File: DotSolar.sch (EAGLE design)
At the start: 24 parts, among them IC1 CAT24M010TS, IC2 SI1145, Q1 BSH203, U1 ISL29125

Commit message: Update tracks for production at Aisler
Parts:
- D1: value (none) -> B130-13-F
- D3: value (none) -> 3.3V
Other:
- note added: "10-50mV Drop"
- note added: "200mV Drop"
- note removed: "100mV Drop"
- note removed: "50mV Drop"
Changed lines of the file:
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@@
 <part name="R2" library="rcl" deviceset="R-EU_" device="R0603" value="4.7kΩ"/>
 <part name="R3" library="rcl" deviceset="R-EU_" device="R0603" value="4.7kΩ"/>
-<part name="D3" library="diode" deviceset="ZENER-DIODE" device="SMB"/>
+<part name="D3" library="diode" deviceset="ZENER-DIODE" device="SMB" value="3.3V"/>
 <part name="Q1" library="BSH203" deviceset="BSH203" device=""/>
 <part name="U1" library="SparkFun-Sensors" deviceset="ISL29125" device=""/>
@@
 <part name="U$5" library="redan" deviceset="INA226" device=""/>
 <part name="R4" library="rcl" deviceset="R-EU_" device="R0603" value="4.7kΩ"/>
-<part name="D1" library="PP_Passives" deviceset="DIODE" device="_B130-13-F"/>
+<part name="D1" library="PP_Passives" deviceset="DIODE" device="_B130-13-F" value="B130-13-F"/>
 <part name="JP2" library="SparkFun-Jumpers" deviceset="JUMPER-SMT_2_NO" device="_SILK" value="NoBattery, only Capacitor"/>
 <part name="U$6" library="IXYS_Solar_cells" deviceset="KXOB22-01X8F_EXTENDED_PADS" device=""/>
@@
 <sheet>
 <plain>
-<text x="86.36" y="66.04" size="1.016" layer="91">50mV Drop</text>
-<text x="93.98" y="60.96" size="1.016" layer="91">100mV Drop</text>
+<text x="86.36" y="66.04" size="0.6096" layer="91">10-50mV Drop</text>
+<text x="93.98" y="60.96" size="0.6096" layer="91">200mV Drop</text>
 <text x="175.26" y="78.74" size="1.778" layer="91">Pullups</text>
 <text x="149.86" y="111.76" size="1.778" layer="91">Address 0x52 and 0x53(upper)</text>

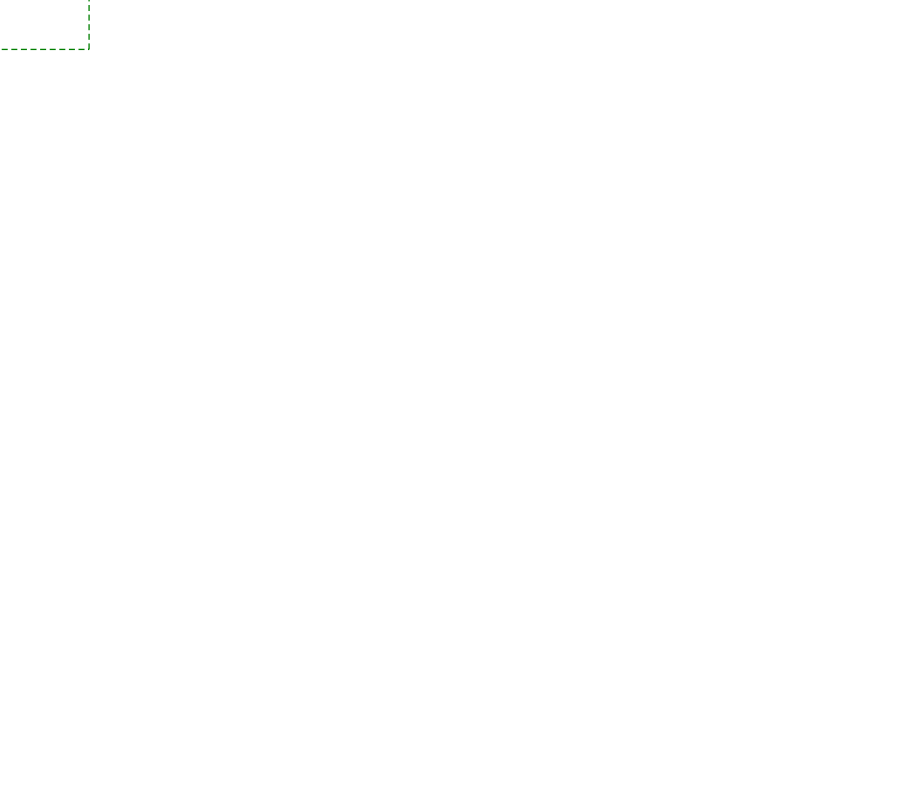
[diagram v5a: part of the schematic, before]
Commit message: Add AS3935 lightning detector
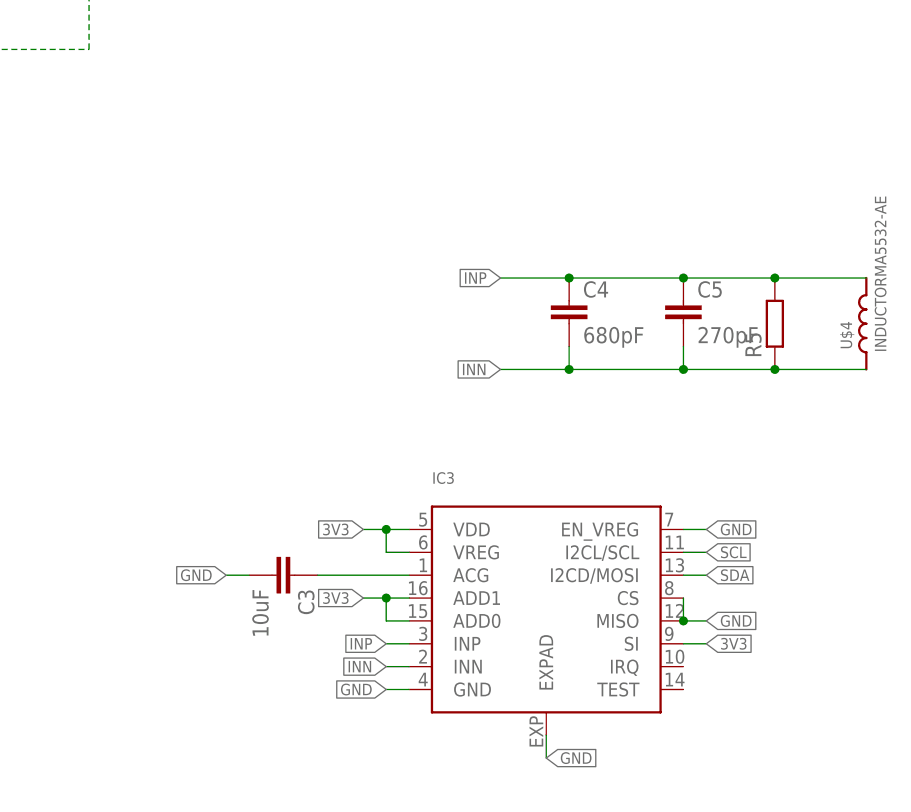
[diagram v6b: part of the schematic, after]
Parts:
- added C3: 10uF, rcl:C-EUC0603
- added C4: 680pF, rcl:C-EUC0603
- added C5: 270pF, rcl:C-EUC0603
- added IC3: (no value), AS3935:AS3935
- added R5: (no value), rcl:R-EU_R0603
- added U$4: INDUCTORMA5532-AE, arducorder-mini:INDUCTORMA5532-AE
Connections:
- new net INN: C4.2, C5.2, IC3.INN, R5.1, U$4.2
- new net INP: C4.1, C5.1, IC3.INP, R5.2, U$4.1
- new net N$3: C3.1, IC3.ACG
- net 3V3: now also IC3.ADD0, IC3.ADD1, IC3.SI, IC3.VDD, IC3.VREG
- net GND: now also C3.2, IC3.CS, IC3.EN_VREG, IC3.EXPAD, IC3.GND, IC3.MISO
- net SCL: now also IC3.I2CL/SCL
- net SDA: now also IC3.I2CD/MOSI
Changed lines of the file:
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@@
 <part name="SJ4" library="SparkFun" deviceset="SOLDERJUMPER_2WAY" device="PASTE2&amp;3"/>
 <part name="JP3" library="SparkFun-Jumpers" deviceset="JUMPER-SMT_3_1-NC_TRACE" device="_SILK"/>
+<part name="IC3" library="AS3935" deviceset="AS3935" device=""/>
+<part name="C3" library="rcl" deviceset="C-EU" device="C0603" value="10uF"/>
+<part name="C4" library="rcl" deviceset="C-EU" device="C0603" value="680pF"/>
+<part name="C5" library="rcl" deviceset="C-EU" device="C0603" value="270pF"/>
+<part name="R5" library="rcl" deviceset="R-EU_" device="R0603"/>
+<part name="U$4" library="arducorder-mini" deviceset="INDUCTOR" device="MA5532-AE"/>
 </parts>
 <sheets>
@@
 <instance part="SJ4" gate="G$1" x="53.34" y="-30.48" rot="R180"/>
 <instance part="JP3" gate="G$1" x="22.86" y="-30.48" rot="R180"/>
+<instance part="IC3" gate="IC" x="220.98" y="-7.62"/>
+<instance part="C3" gate="G$1" x="208.28" y="-12.7" rot="R270"/>
+<instance part="C4" gate="G$1" x="238.76" y="17.78"/>
+<instance part="C5" gate="G$1" x="251.46" y="17.78"/>
+<instance part="R5" gate="G$1" x="261.62" y="15.24" rot="R90"/>
+<instance part="U$4" gate="G$1" x="271.78" y="15.24"/>
 </instances>
 <busses>
@@
 <label x="48.26" y="-35.56" size="1.27" layer="95" rot="R180" xref="yes"/>
 </segment>
+<segment>
+<pinref part="C3" gate="G$1" pin="2"/>
+<wire x1="203.2" y1="-12.7" x2="200.66" y2="-12.7" width="0.1524" layer="91"/>
+<label x="200.66" y="-12.7" size="1.27" layer="95" rot="R180" xref="yes"/>
+</segment>
+<segment>
+<pinref part="IC3" gate="IC" pin="GND"/>
+<wire x1="220.98" y1="-25.4" x2="218.44" y2="-25.4" width="0.1524" layer="91"/>
+<label x="218.44" y="-25.4" size="1.27" layer="95" rot="R180" xref="yes"/>
+</segment>
+<segment>
+<pinref part="IC3" gate="IC" pin="EN_VREG"/>
+<wire x1="251.46" y1="-7.62" x2="254" y2="-7.62" width="0.1524" layer="91"/>
+<label x="254" y="-7.62" size="1.27" layer="95" xref="yes"/>
+</segment>
+<segment>
+<pinref part="IC3" gate="IC" pin="CS"/>
+<pinref part="IC3" gate="IC" pin="MISO"/>
+<wire x1="251.46" y1="-15.24" x2="251.46" y2="-17.78" width="0.1524" layer="91"/>
+<wire x1="251.46" y1="-17.78" x2="254" y2="-17.78" width="0.1524" layer="91"/>
+<junction x="251.46" y="-17.78"/>
+<label x="254" y="-17.78" size="1.27" layer="95" xref="yes"/>
+</segment>
+<segment>
+<pinref part="IC3" gate="IC" pin="EXPAD"/>
+<wire x1="236.22" y1="-30.48" x2="236.22" y2="-33.02" width="0.1524" layer="91"/>
+<label x="236.22" y="-33.02" size="1.27" layer="95" xref="yes"/>
+</segment>
 </net>
 <net name="3V3" class="0">
@@
 <label x="48.26" y="-25.4" size="1.27" layer="95" rot="R180" xref="yes"/>
 </segment>
+<segment>
+<pinref part="IC3" gate="IC" pin="ADD1"/>
+<wire x1="220.98" y1="-15.24" x2="218.44" y2="-15.24" width="0.1524" layer="91"/>
+<pinref part="IC3" gate="IC" pin="ADD0"/>
+<wire x1="218.44" y1="-15.24" x2="215.9" y2="-15.24" width="0.1524" layer="91"/>
+<wire x1="220.98" y1="-17.78" x2="218.44" y2="-17.78" width="0.1524" layer="91"/>
+<wire x1="218.44" y1="-17.78" x2="218.44" y2="-15.24" width="0.1524" layer="91"/>
+<junction x="218.44" y="-15.24"/>
+<label x="215.9" y="-15.24" size="1.27" layer="95" rot="R180" xref="yes"/>
+</segment>
+<segment>
+<pinref part="IC3" gate="IC" pin="VREG"/>
+<wire x1="220.98" y1="-10.16" x2="218.44" y2="-10.16" width="0.1524" layer="91"/>
+<pinref part="IC3" gate="IC" pin="VDD"/>
+<wire x1="220.98" y1="-7.62" x2="218.44" y2="-7.62" width="0.1524" layer="91"/>
+<wire x1="218.44" y1="-7.62" x2="218.44" y2="-10.16" width="0.1524" layer="91"/>
+<wire x1="218.44" y1="-7.62" x2="215.9" y2="-7.62" width="0.1524" layer="91"/>
+<junction x="218.44" y="-7.62"/>
+<label x="215.9" y="-7.62" size="1.27" layer="95" rot="R180" xref="yes"/>
+</segment>
+<segment>
+<pinref part="IC3" gate="IC" pin="SI"/>
+<wire x1="251.46" y1="-20.32" x2="254" y2="-20.32" width="0.1524" layer="91"/>
+<label x="254" y="-20.32" size="1.27" layer="95" xref="yes"/>
+</segment>
 </net>
 <net name="A0" class="0">
@@
 <label x="139.7" y="104.14" size="1.27" layer="95" rot="R180" xref="yes"/>
 </segment>
+<segment>
+<pinref part="IC3" gate="IC" pin="I2CD/MOSI"/>
+<wire x1="251.46" y1="-12.7" x2="254" y2="-12.7" width="0.1524" layer="91"/>
+<label x="254" y="-12.7" size="1.27" layer="95" xref="yes"/>
+</segment>
 </net>
 <net name="SCL" class="0">
@@
 <wire x1="147.32" y1="101.6" x2="139.7" y2="101.6" width="0.1524" layer="91"/>
 <label x="139.7" y="101.6" size="1.27" layer="95" rot="R180" xref="yes"/>
+</segment>
+<segment>
+<pinref part="IC3" gate="IC" pin="I2CL/SCL"/>
+<wire x1="251.46" y1="-10.16" x2="254" y2="-10.16" width="0.1524" layer="91"/>
+<label x="254" y="-10.16" size="1.27" layer="95" xref="yes"/>
 </segment>
 </net>
@@
 </segment>
 </net>
+<net name="N$3" class="0">
+<segment>
+<pinref part="IC3" gate="IC" pin="ACG"/>
+<pinref part="C3" gate="G$1" pin="1"/>
+<wire x1="220.98" y1="-12.7" x2="210.82" y2="-12.7" width="0.1524" layer="91"/>
+</segment>
+</net>
+<net name="INP" class="0">
+<segment>
+<pinref part="IC3" gate="IC" pin="INP"/>
+<wire x1="220.98" y1="-20.32" x2="218.44" y2="-20.32" width="0.1524" layer="91"/>
+<label x="218.44" y="-20.32" size="1.27" layer="95" rot="R180" xref="yes"/>
+</segment>
+<segment>
+<wire x1="231.14" y1="20.32" x2="238.76" y2="20.32" width="0.1524" layer="91"/>
+<label x="231.14" y="20.32" size="1.27" layer="95" rot="R180" xref="yes"/>
+<pinref part="C4" gate="G$1" pin="1"/>
+<pinref part="C5" gate="G$1" pin="1"/>
+<wire x1="238.76" y1="20.32" x2="251.46" y2="20.32" width="0.1524" layer="91"/>
+<junction x="238.76" y="20.32"/>
+<wire x1="251.46" y1="20.32" x2="261.62" y2="20.32" width="0.1524" layer="91"/>
+<junction x="251.46" y="20.32"/>
+<pinref part="R5" gate="G$1" pin="2"/>
+<junction x="261.62" y="20.32"/>
+<pinref part="U$4" gate="G$1" pin="1"/>
+<wire x1="271.78" y1="20.32" x2="261.62" y2="20.32" width="0.1524" layer="91"/>
+</segment>
+</net>
+<net name="INN" class="0">
+<segment>
+<pinref part="IC3" gate="IC" pin="INN"/>
+<wire x1="220.98" y1="-22.86" x2="218.44" y2="-22.86" width="0.1524" layer="91"/>
+<label x="218.44" y="-22.86" size="1.27" layer="95" rot="R180" xref="yes"/>
+</segment>
+<segment>
+<pinref part="R5" gate="G$1" pin="1"/>
+<wire x1="238.76" y1="10.16" x2="251.46" y2="10.16" width="0.1524" layer="91"/>
+<pinref part="C5" gate="G$1" pin="2"/>
+<wire x1="251.46" y1="10.16" x2="261.62" y2="10.16" width="0.1524" layer="91"/>
+<wire x1="251.46" y1="12.7" x2="251.46" y2="10.16" width="0.1524" layer="91"/>
+<junction x="251.46" y="10.16"/>
+<pinref part="C4" gate="G$1" pin="2"/>
+<wire x1="238.76" y1="12.7" x2="238.76" y2="10.16" width="0.1524" layer="91"/>
+<wire x1="238.76" y1="10.16" x2="231.14" y2="10.16" width="0.1524" layer="91"/>
+<junction x="238.76" y="10.16"/>
+<label x="231.14" y="10.16" size="1.27" layer="95" rot="R180" xref="yes"/>
+<junction x="261.62" y="10.16"/>
+<pinref part="U$4" gate="G$1" pin="2"/>
+<wire x1="261.62" y1="10.16" x2="271.78" y2="10.16" width="0.1524" layer="91"/>
+</segment>
+</net>
